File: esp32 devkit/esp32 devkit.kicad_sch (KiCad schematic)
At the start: 13 parts, among them U1 ESP32-WROOM-32E

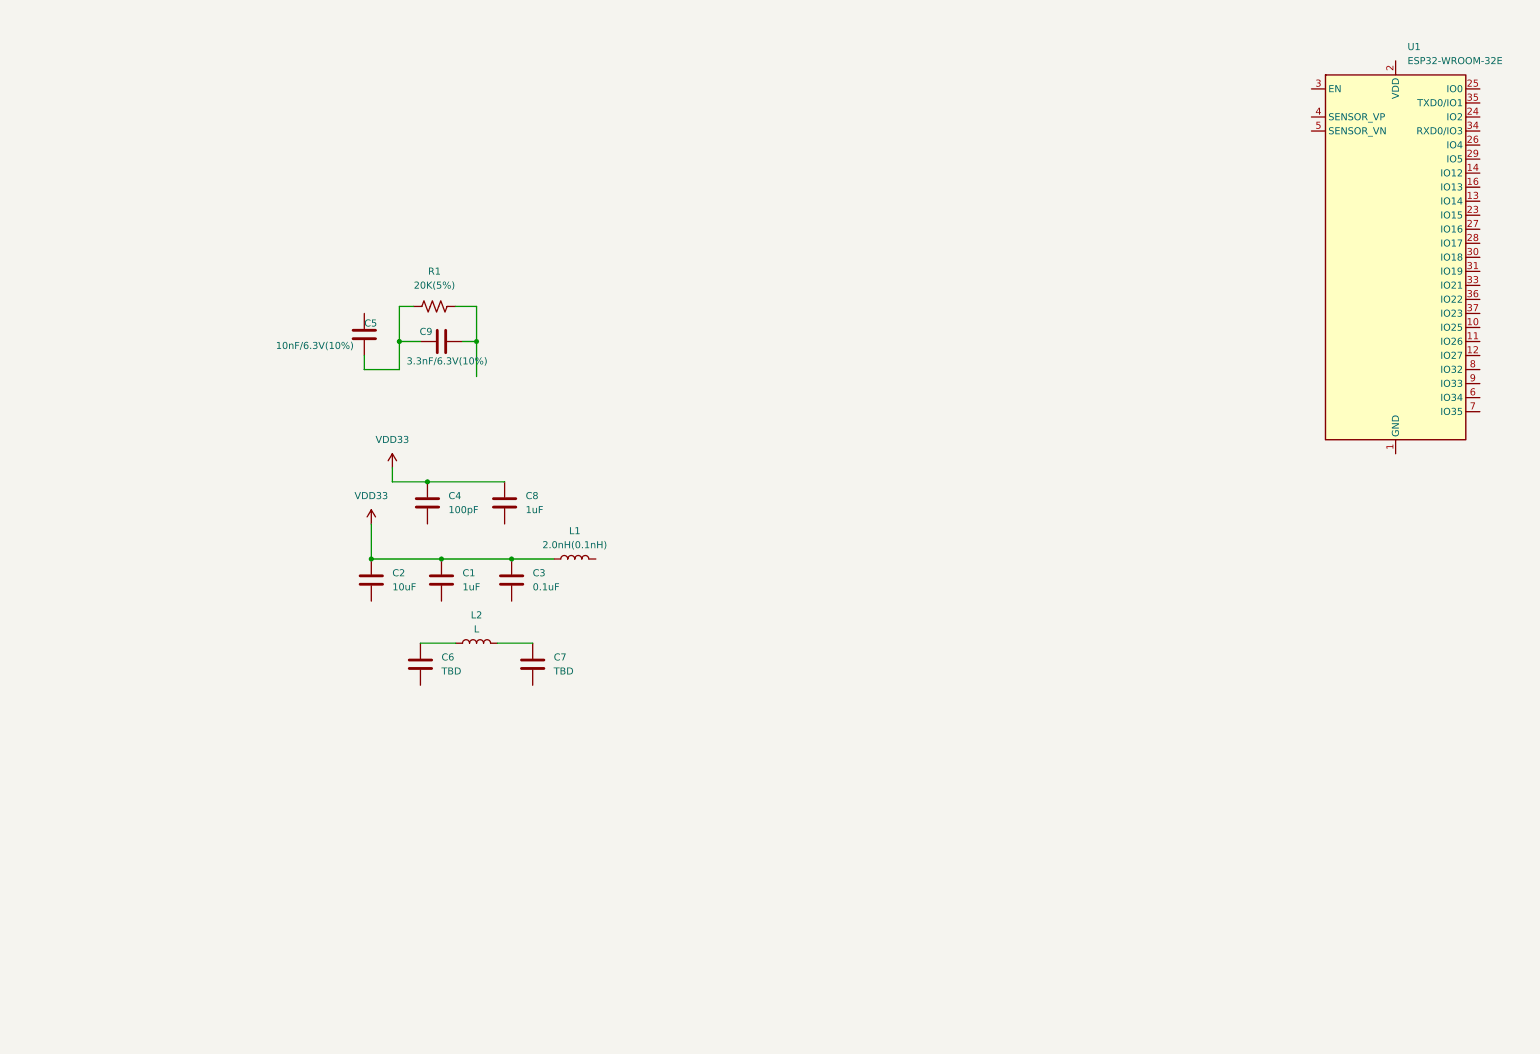
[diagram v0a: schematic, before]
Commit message: :construction: ADDED USB TYP C N UART
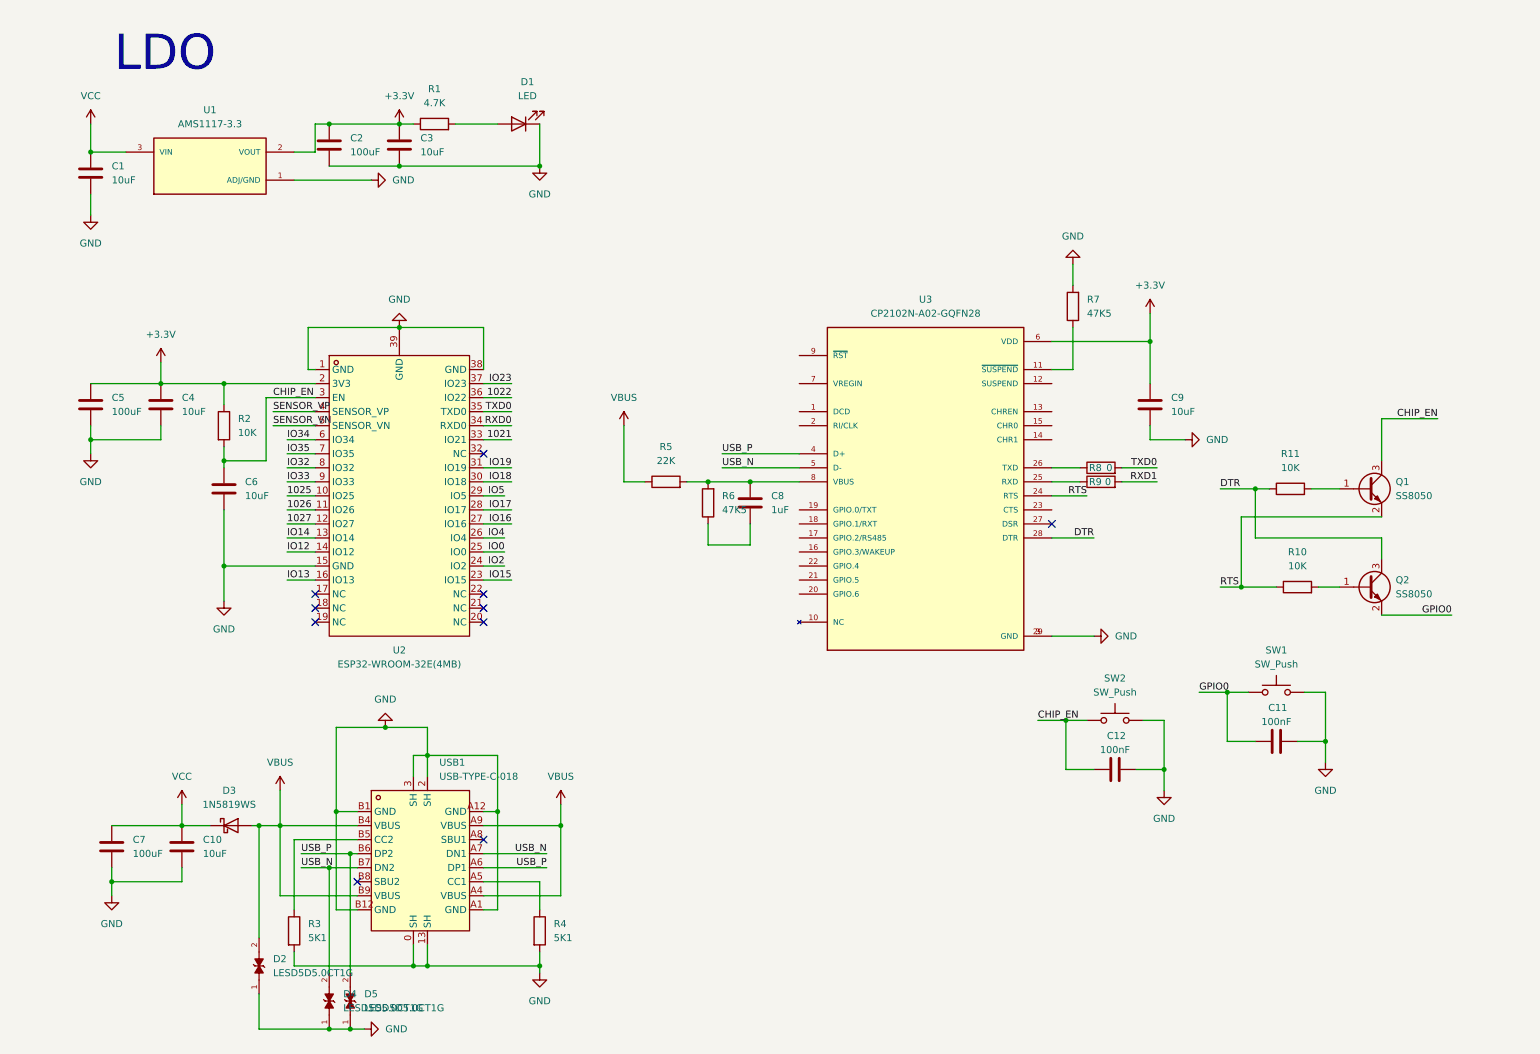
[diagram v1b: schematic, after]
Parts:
- removed L1: 2.0nH(0.1nH), Inductor_THT:L_Axial_L9.5mm_D4.0mm_P5.08mm_Vertical_Fastron_SMCC, symbol Device:L
- removed L2: L, symbol Device:L
- removed R1: 20K(5%), Resistor_THT:R_Axial_DIN0309_L9.0mm_D3.2mm_P12.70mm_Horizontal, symbol Device:R_US
- removed U1: ESP32-WROOM-32E, RF_Module:ESP32-WROOM-32D, symbol RF_Module:ESP32-WROOM-32E
- added C10: 10uF, symbol Device:C
- added C11, C12: 100nF, symbol Device:C
- added D1: LED, symbol Device:LED
- added D2, D4, D5: LESD5D5.0CT1G, LESD5D5.0CT1G:TVS_LESD5D5.0CT1G, symbol LESD5D5.0CT1G:LESD5D5.0CT1G
- added D3: 1N5819WS, Diode_SMD:D_SOD-323, symbol Diode:1N5819WS
- added Q1, Q2: SS8050, Package_TO_SOT_SMD:SOT-23, symbol Transistor_BJT:SS8050
- added R1: 4.7K, symbol Device:R
- added R10, R11, R2: 10K, symbol Device:R
- added R3, R4: 5K1, symbol Device:R
- added R5: 22K, symbol Device:R
- added R6, R7: 47K5, symbol Device:R
- added R8, R9: 0, symbol Device:R
- added SW1, SW2: SW_Push, symbol Switch:SW_Push
- added U1: AMS1117-3.3, AMS1117-3.3:SOT229P700X180-4N, symbol AMS1117-3.3:AMS1117-3.3
- added U2: ESP32-WROOM-32E(4MB), ESP32-WROOM-32E-N4:WIFI-SMD_ESP32-WROOM-32E, symbol ESP32-WROOM-32E-N4:ESP32-WROOM-32E(4MB)
- added U3: CP2102N-A02-GQFN28, CP2102N-A02-GQFN28:QFN50P500X500X80-29N, symbol CP2102N-A02-GQFN28:CP2102N-A02-GQFN28
- added USB1: USB-TYPE-C-018, USB-TYPE-C-018:USB-C_SMD-TYPE-C-31-M-12, symbol Usb_type_c_018:USB-TYPE-C-018
- C1: value 1uF -> 10uF; footprint Capacitor_SMD:C_1206_3216Metric -> (none)
- C2: value 10uF -> 100uF; footprint Capacitor_SMD:C_1206_3216Metric -> (none)
- C3: value 0.1uF -> 10uF; footprint Capacitor_SMD:C_1206_3216Metric -> (none)
- C4: value 100pF -> 10uF; footprint Capacitor_SMD:C_1812_4532Metric_Pad1.57x3.40mm_HandSolder -> (none)
- C5: value 10nF/6.3V(10%) -> 100uF; footprint Capacitor_SMD:C_1206_3216Metric -> (none)
- C6: value TBD -> 10uF
- C7: value TBD -> 100uF
- C8: footprint Capacitor_SMD:C_1206_3216Metric -> (none)
- C9: value 3.3nF/6.3V(10%) -> 10uF; footprint Capacitor_SMD:C_1206_3216Metric -> (none)
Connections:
- net CHIP_EN: now reaches C6.1
- net CHIP_EN: now also C12.2, Q1.3 (C), R2.2, SW2.1, U2.3 (EN)
- net GND: now reaches C6.2
- net GND: now also C1.2, C2.1, C3.2, C4.2, C5.1, C7.1, C9.2, C10.2, C11.1, C12.1, D1.1 (K), D2.1, D4.1, D5.1, R3.2, R4.2, R7.2, SW1.2, SW2.2, U1.1 (ADJ/GND), U2.1 (GND), U2.15 (GND), U2.38 (GND), U2.39 (GND), U3.29 (GND), U3.3 (GND), USB1.0 (SH), USB1.13 (SH), USB1.2 (SH), USB1.3 (SH), USB1.A1 (GND), USB1.A12 (GND), USB1.B1 (GND), USB1.B12 (GND)
- net +3.3V: now reaches C5.2, C9.1
- net +3.3V: now also C2.2, C3.1, C4.1, R1.1, R2.1, U1.2 (VOUT), U2.2 (3V3), U3.6 (VDD)
- net VCC: now reaches C7.2
- net VCC: now also C1.1, C10.1, D3.1 (K), U1.3 (VIN)
- net at C8.2: now also R6.1
- removed net VDD33: C1.1, C2.1, C3.1, C4.1, C8.1
- new net: Q2.1 (B), R10.2
- new net: D1.2 (A), R1.2
- new net: R4.1, USB1.A5 (CC1)
- new net: Q1.1 (B), R11.2
- new net: C8.1, R5.2, R6.2, U3.8 (VBUS)
- new net: R7.1, U3.11 (~{SUSPEND})
- new net: R9.1, U3.25 (RXD)
- new net: R8.1, U3.26 (TXD)
- new net: R3.1, USB1.B5 (CC2)
- new net 1021: U2.33 (IO21)
- new net 1022: U2.36 (IO22)
- new net 1025: U2.10 (IO25)
- new net 1026: U2.11 (IO26)
- new net 1027: U2.12 (IO27)
- new net DTR: Q2.3 (C), R11.1, U3.28 (DTR)
- new net GPIO0: C11.2, Q2.2 (E), SW1.1
- new net IO0: U2.25 (IO0)
- new net IO12: U2.14 (IO12)
- new net IO13: U2.16 (IO13)
- new net IO14: U2.13 (IO14)
- new net IO15: U2.23 (IO15)
- new net IO16: U2.27 (IO16)
- new net IO17: U2.28 (IO17)
- new net IO18: U2.30 (IO18)
- new net IO19: U2.31 (IO19)
- new net IO2: U2.24 (IO2)
- new net IO23: U2.37 (IO23)
- new net IO32: U2.8 (IO32)
- new net IO33: U2.9 (IO33)
- new net IO34: U2.6 (IO34)
- new net IO35: U2.7 (IO35)
- new net IO4: U2.26 (IO4)
- new net IO5: U2.29 (IO5)
- new net RTS: Q1.2 (E), R10.1, U3.24 (RTS)
- new net RXD0: U2.34 (RXD0)
- new net RXD1: R9.2
- new net SENSOR_VN: U2.5 (SENSOR_VN)
- new net SENSOR_VP: U2.4 (SENSOR_VP)
- new net TXD0: R8.2, U2.35 (TXD0)
- new net USB_N: D4.2, U3.5 (D-), USB1.A7 (DN1), USB1.B7 (DN2)
- new net USB_P: D5.2, U3.4 (D+), USB1.A6 (DP1), USB1.B6 (DP2)
- new net VBUS: D2.2, D3.2 (A), R5.1, USB1.A4 (VBUS), USB1.A9 (VBUS), USB1.B4 (VBUS), USB1.B9 (VBUS)
- no-connect marks 0 -> 10
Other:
- note added: "LDO"

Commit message: :green_heart: completing the connectors
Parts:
- added J1, J2: Conn_01x19, symbol Connector_Generic:Conn_01x19
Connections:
- net 1021: now also J2.5 (Pin_5)
- net 1022: now also J2.2 (Pin_2)
- net 1025: now also J1.9 (Pin_9)
- net 1026: now also J1.10 (Pin_10)
- net 1027: now also J1.11 (Pin_11)
- net IO0: now also J2.13 (Pin_13)
- net IO12: now also J1.13 (Pin_13)
- net IO13: now also J1.15 (Pin_15)
- net IO14: now also J1.12 (Pin_12)
- net IO15: now also J2.15 (Pin_15)
- net IO16: now also J2.11 (Pin_11)
- net IO17: now also J2.10 (Pin_10)
- net IO18: now also J2.8 (Pin_8)
- net IO19: now also J2.7 (Pin_7)
- net IO2: now also J2.14 (Pin_14)
- net IO23: now also J2.1 (Pin_1)
- net IO32: now also J1.7 (Pin_7)
- net IO33: now also J1.8 (Pin_8)
- net IO34: now also J1.5 (Pin_5)
- net IO35: now also J1.6 (Pin_6)
- net IO4: now also J2.12 (Pin_12)
- net IO5: now also J2.9 (Pin_9)
- net RXD0: now also J2.4 (Pin_4)
- net SENSOR_VN: now also J1.4 (Pin_4)
- net SENSOR_VP: now also J1.3 (Pin_3)
- net TXD0: now also J2.3 (Pin_3)
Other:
- moved on the sheet: C11, C12, C8, C9, Q1, Q2, R10, R11, R5, R6, R7, R8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

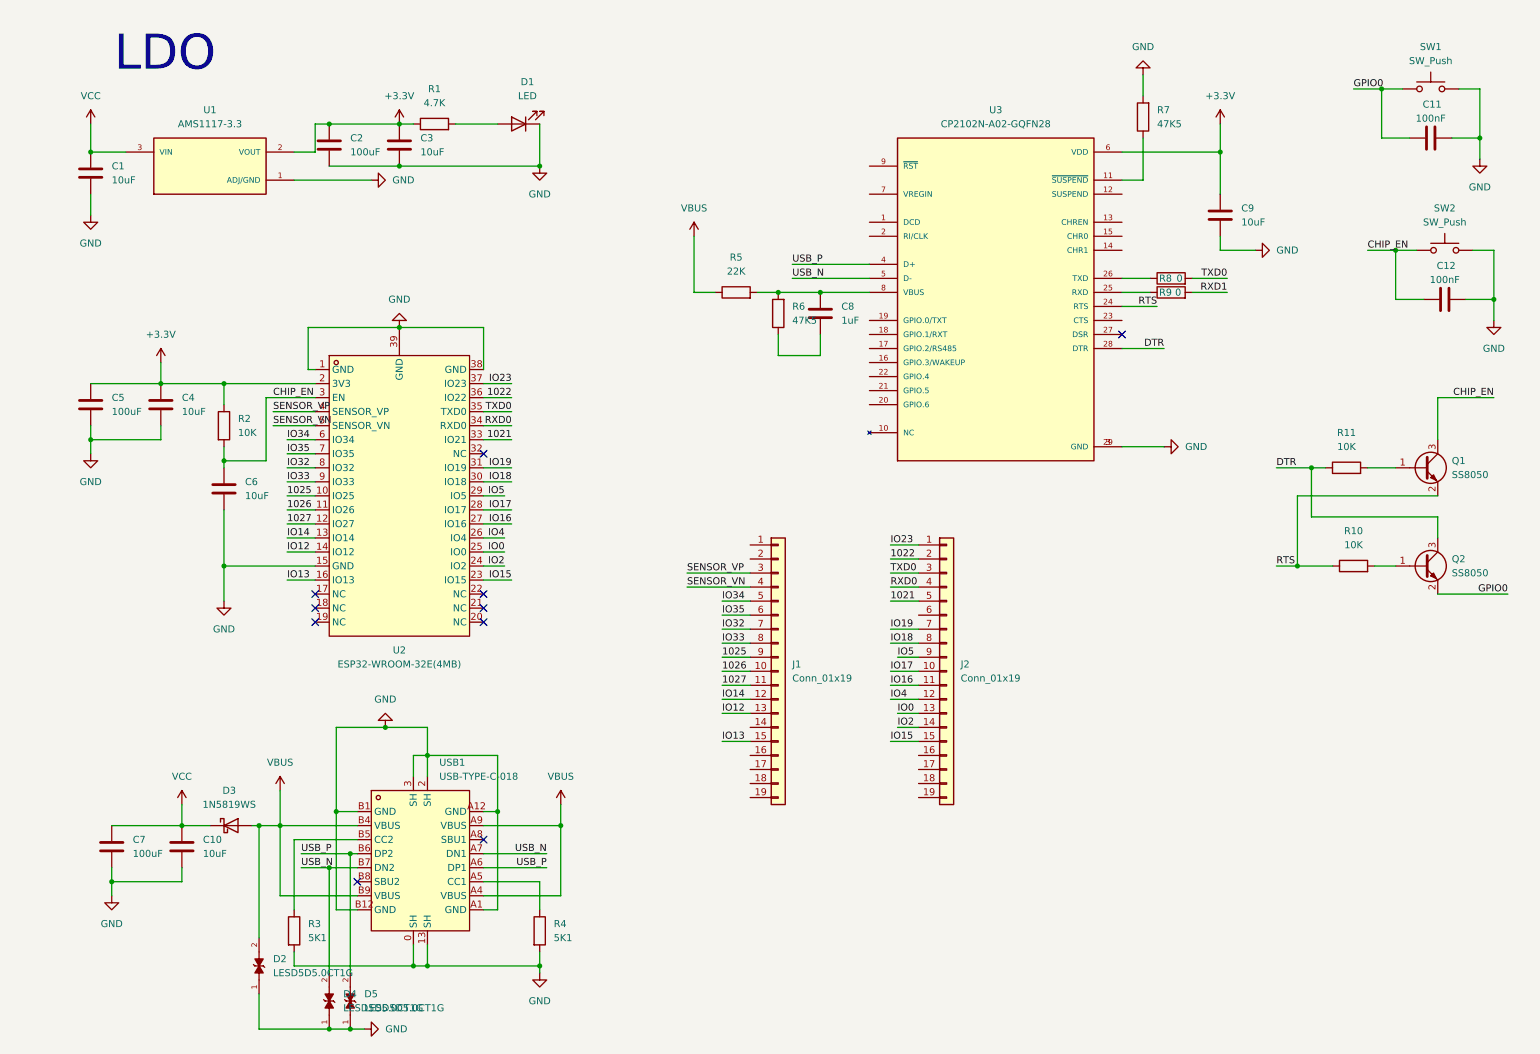
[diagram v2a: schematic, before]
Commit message: :rocket: completed electrical checker rules
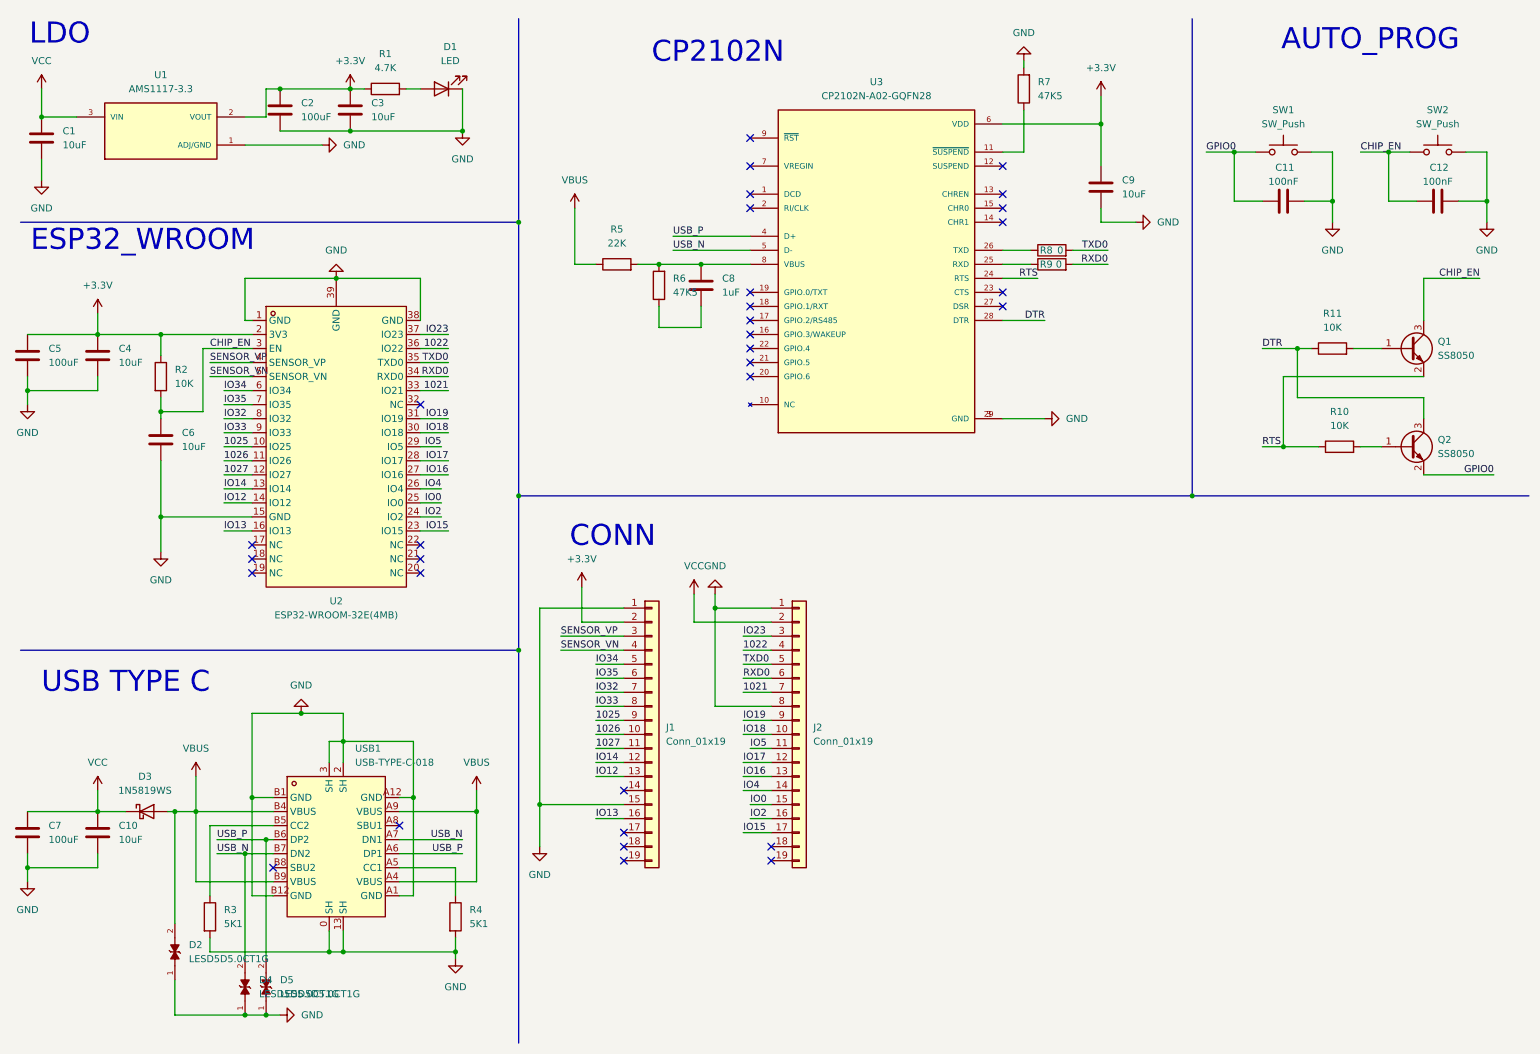
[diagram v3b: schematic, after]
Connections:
- net RXD1 is gone; now on net RXD0: R9.2
- net +3.3V: now also J1.2 (Pin_2)
- net 1021: now also J2.7 (Pin_7); no longer J2.5 (Pin_5)
- net 1022: now also J2.4 (Pin_4); no longer J2.2 (Pin_2)
- net GND: now also J1.1 (Pin_1), J1.15 (Pin_15), J2.1 (Pin_1), J2.8 (Pin_8)
- net IO0: now also J2.15 (Pin_15); no longer J2.13 (Pin_13)
- net IO13: now also J1.16 (Pin_16); no longer J1.15 (Pin_15)
- net IO15: now also J2.17 (Pin_17); no longer J2.15 (Pin_15)
- net IO16: now also J2.13 (Pin_13); no longer J2.11 (Pin_11)
- net IO17: now also J2.12 (Pin_12); no longer J2.10 (Pin_10)
- net IO18: now also J2.10 (Pin_10); no longer J2.8 (Pin_8)
- net IO19: now also J2.9 (Pin_9); no longer J2.7 (Pin_7)
- net IO2: now also J2.16 (Pin_16); no longer J2.14 (Pin_14)
- net IO23: now also J2.3 (Pin_3); no longer J2.1 (Pin_1)
- net IO4: now also J2.14 (Pin_14); no longer J2.12 (Pin_12)
- net IO5: now also J2.11 (Pin_11); no longer J2.9 (Pin_9)
- net RXD0: now also J2.6 (Pin_6); no longer J2.4 (Pin_4)
- net TXD0: now also J2.5 (Pin_5); no longer J2.3 (Pin_3)
- net VCC: now also J2.2 (Pin_2)
- no-connect marks 10 -> 32
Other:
- note added: "AUTO_PROG"
- note added: "CONN"
- note added: "CP2102N"
- note added: "ESP32_WROOM"
- note added: "USB TYPE C"
- moved on the sheet: C1, C10, C11, C12, C2, C3, C4, C5, C6, C7, C8, C9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
